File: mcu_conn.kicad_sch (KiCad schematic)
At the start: 12 parts, among them J10 Conn_01x04_Pin, J8 Conn_01x01_Pin, J9 Conn_01x05_Pin, Q6 FDV305N

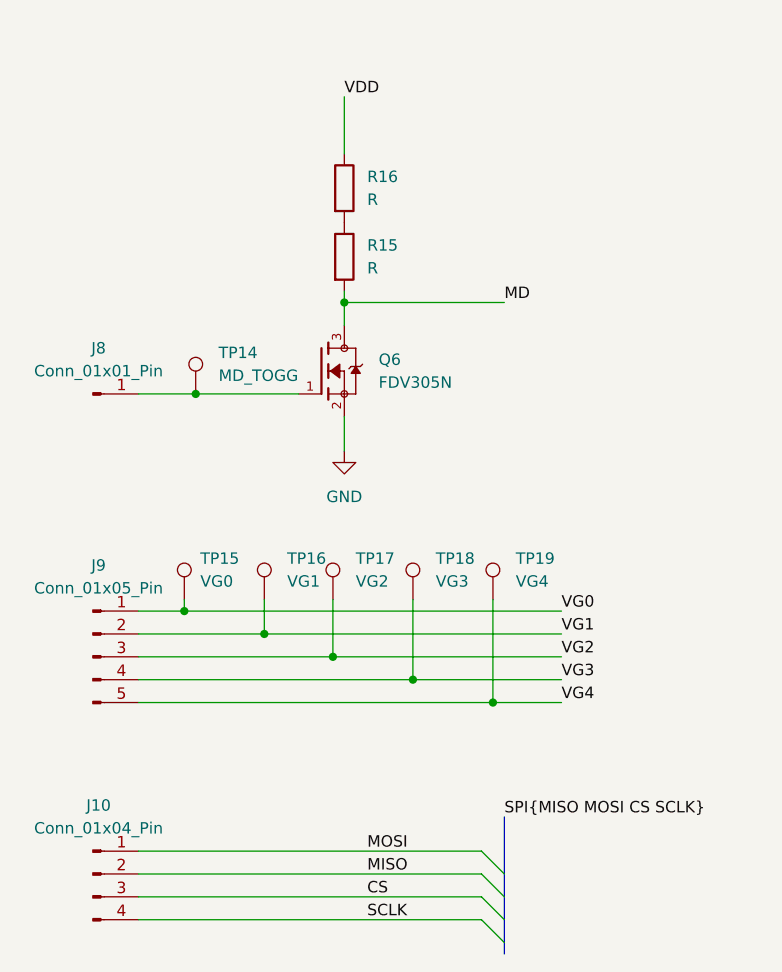
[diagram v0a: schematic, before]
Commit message: Join the gate and mode nets across sheets with global labels
VG0 to VG4 and MD now use global labels on both sheets, so the MCU
header reaches the FET gates and the MD pin. Nets go from 35 to 29
because each pair merged into one.

Adds R17, a gate pull-down for Q6 on the MCU sheet, with no value or
footprint yet. 66 parts.

The MCU sheet's VDD label is still local, so R16 is not on the VDD rail.
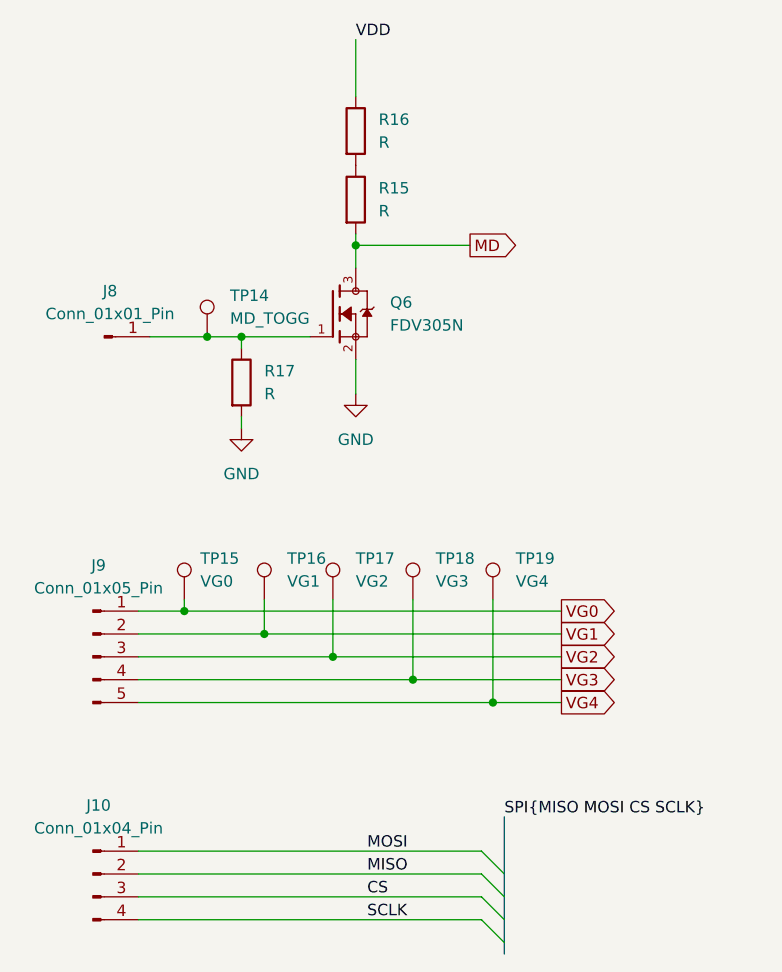
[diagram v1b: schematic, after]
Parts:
- added R17: R, symbol Device:R
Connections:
- net GND: now also R17.2
- net at J8.1 (Pin_1), Q6.1, TP14.1: now also R17.1
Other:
- moved on the sheet: J8, Q6, R15, R16, TP14
